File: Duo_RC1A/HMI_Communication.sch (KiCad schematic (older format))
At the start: 24 parts, among them P1 HEADER_180_2.54_10X2, U1 SN75176BDR

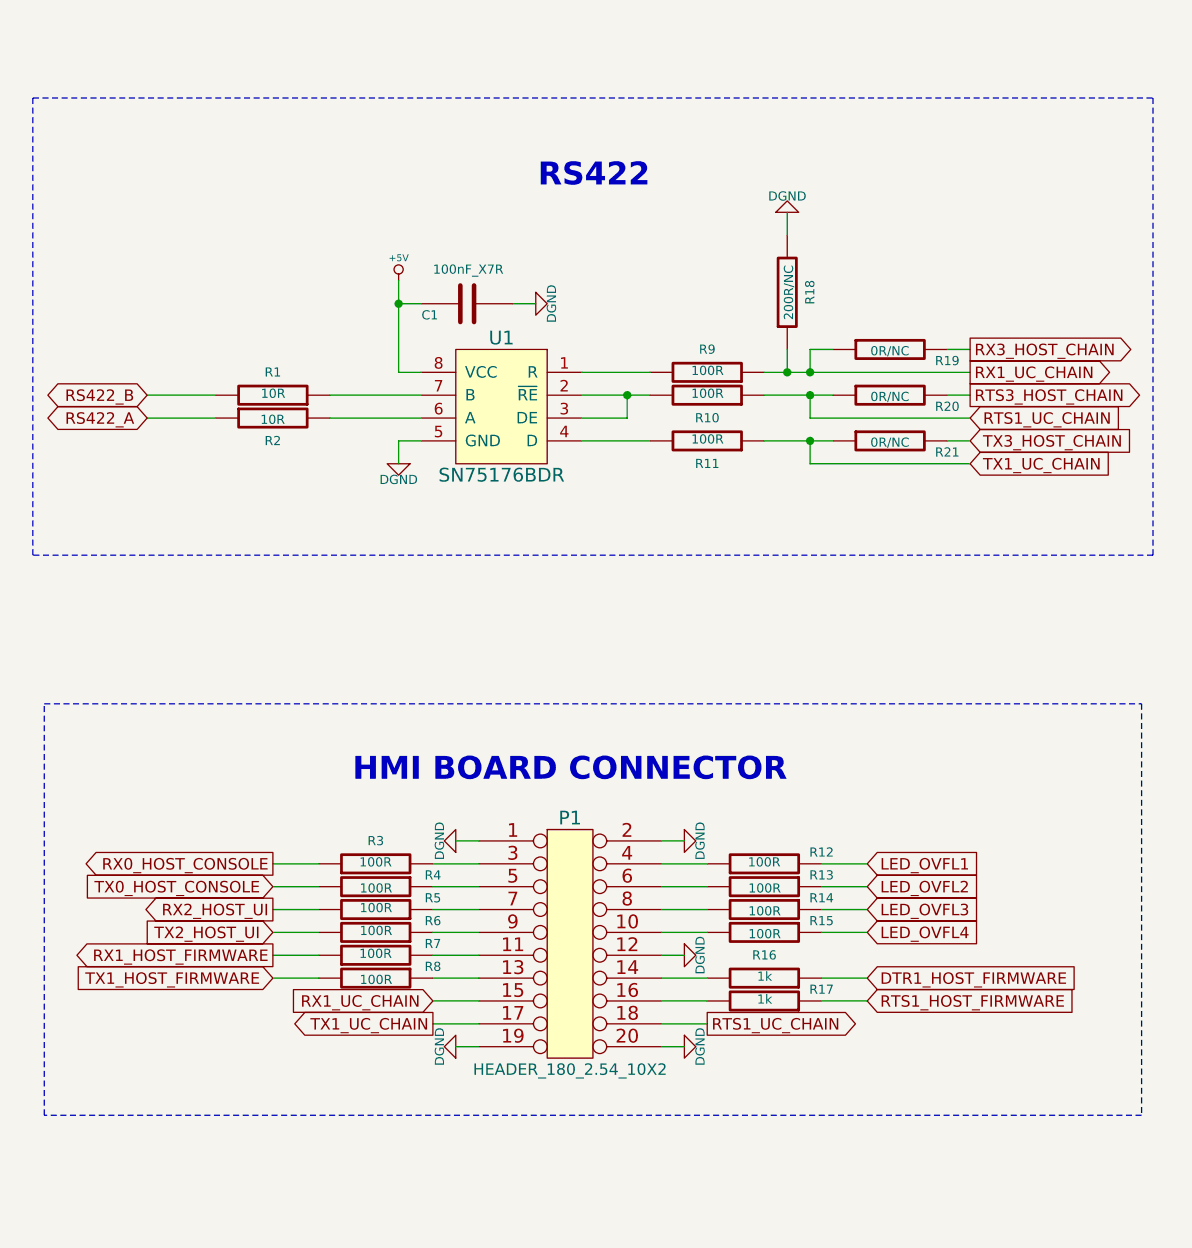
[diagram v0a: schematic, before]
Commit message: Working on the BottomBoard layout. Moved the ITEAD Coreboard to the board left side so there is more space for the linear regulators. Stopped on the USB OTG and USB Host layout.
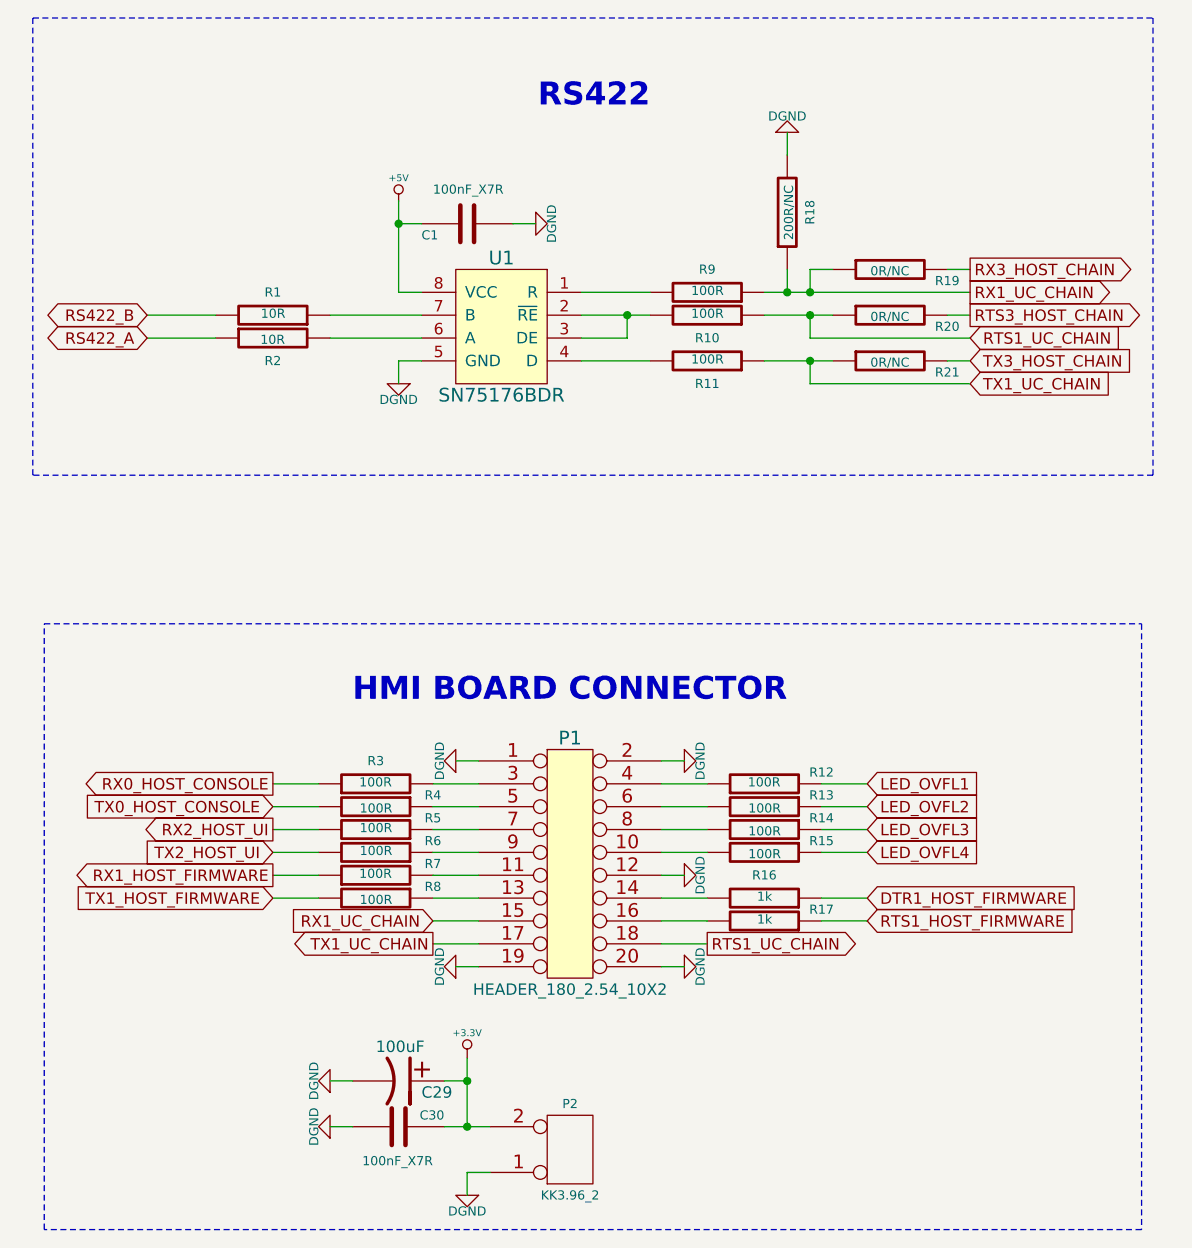
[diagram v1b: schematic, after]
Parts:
- added C29: 100uF, Duo_Audio_HMI_RC1A:Capacitor5x11RM2, symbol CP1
- added C30: 100nF_X7R, Duo_Audio_HMI_RC1A:SM0603, symbol C
- added P2: KK3.96_2, symbol CONN_2
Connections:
- net DGND: now also C29.2, C30.1, P2.1 (P1)
- new net +3.3V: C29.1, C30.2, P2.2 (PM)
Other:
- moved on the sheet: C1, P1, R1, R10, R11, R12, R13, R14, R15, R16, R17, R18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

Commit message: Rear pannel layout finished. First layout of sound modules.
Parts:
- P2: footprint (none) -> Duo_Audio_HMI_RC1A:KK3.96_2PIN
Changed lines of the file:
@@
 F 0 "P2" H 5450 5900 40  0000 C CNN
 F 1 "KK3.96_2" H 5450 6300 40  0000 C CNN
-F 2 "" H 5450 6100 60  0000 C CNN
+F 2 "Duo_Audio_HMI_RC1A:KK3.96_2PIN" H 5450 6100 60  0001 C CNN
 F 3 "" H 5450 6100 60  0000 C CNN
 	1    5450 6100

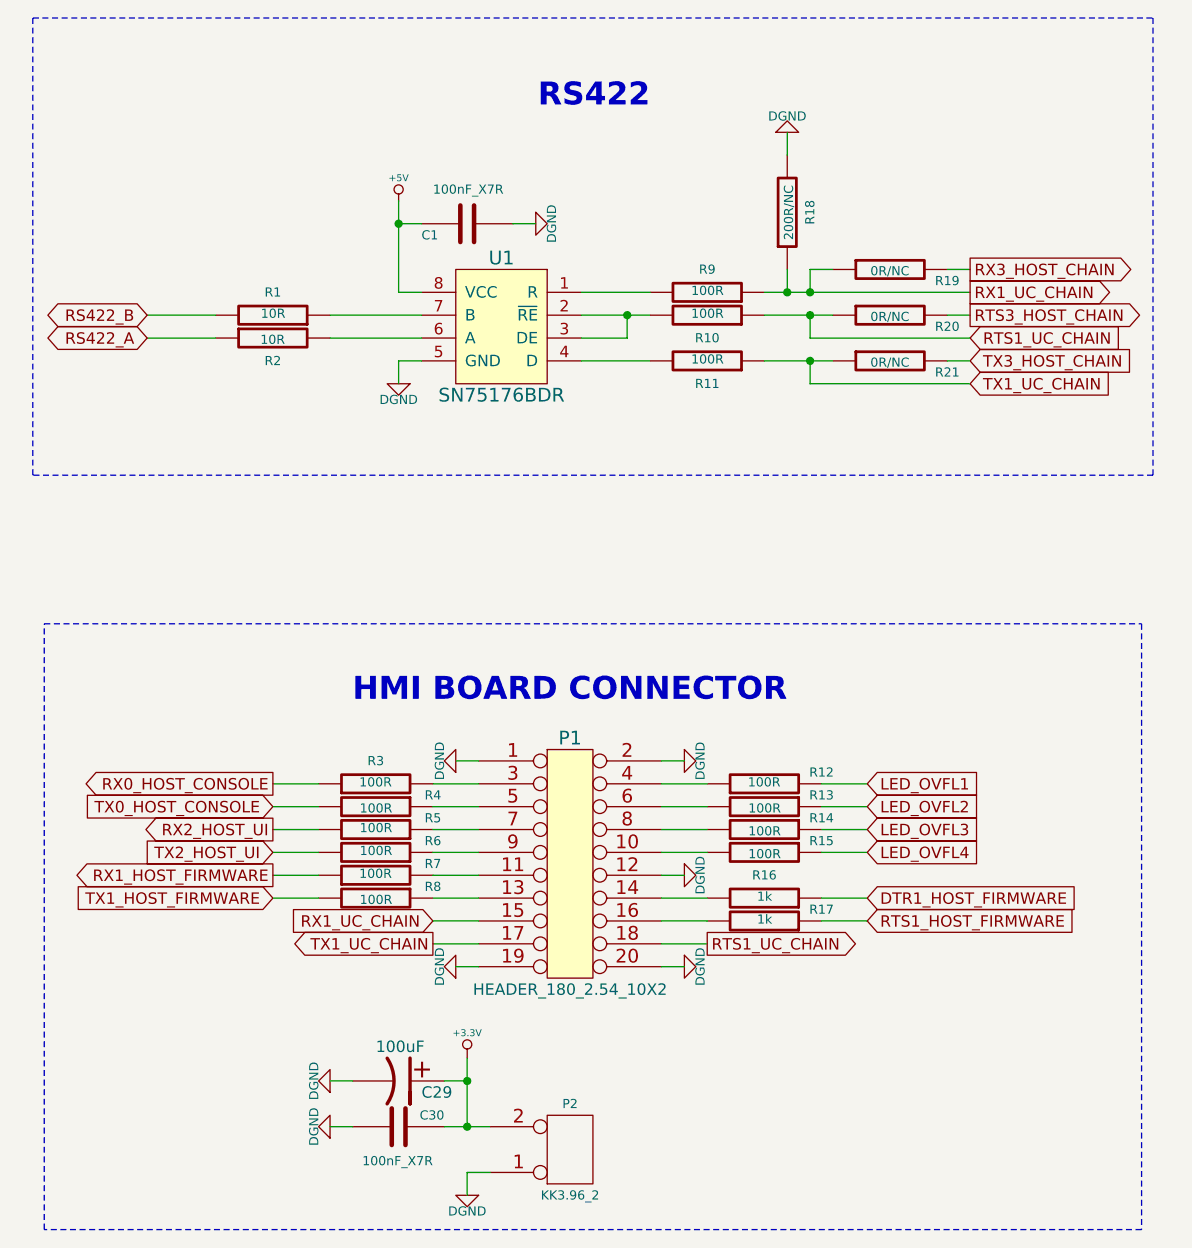
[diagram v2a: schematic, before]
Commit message: Removed CODEC_MITEC signal. Defined the connector between the TopBoard and the BottomBoard. Saved layouts in *.brd old format.
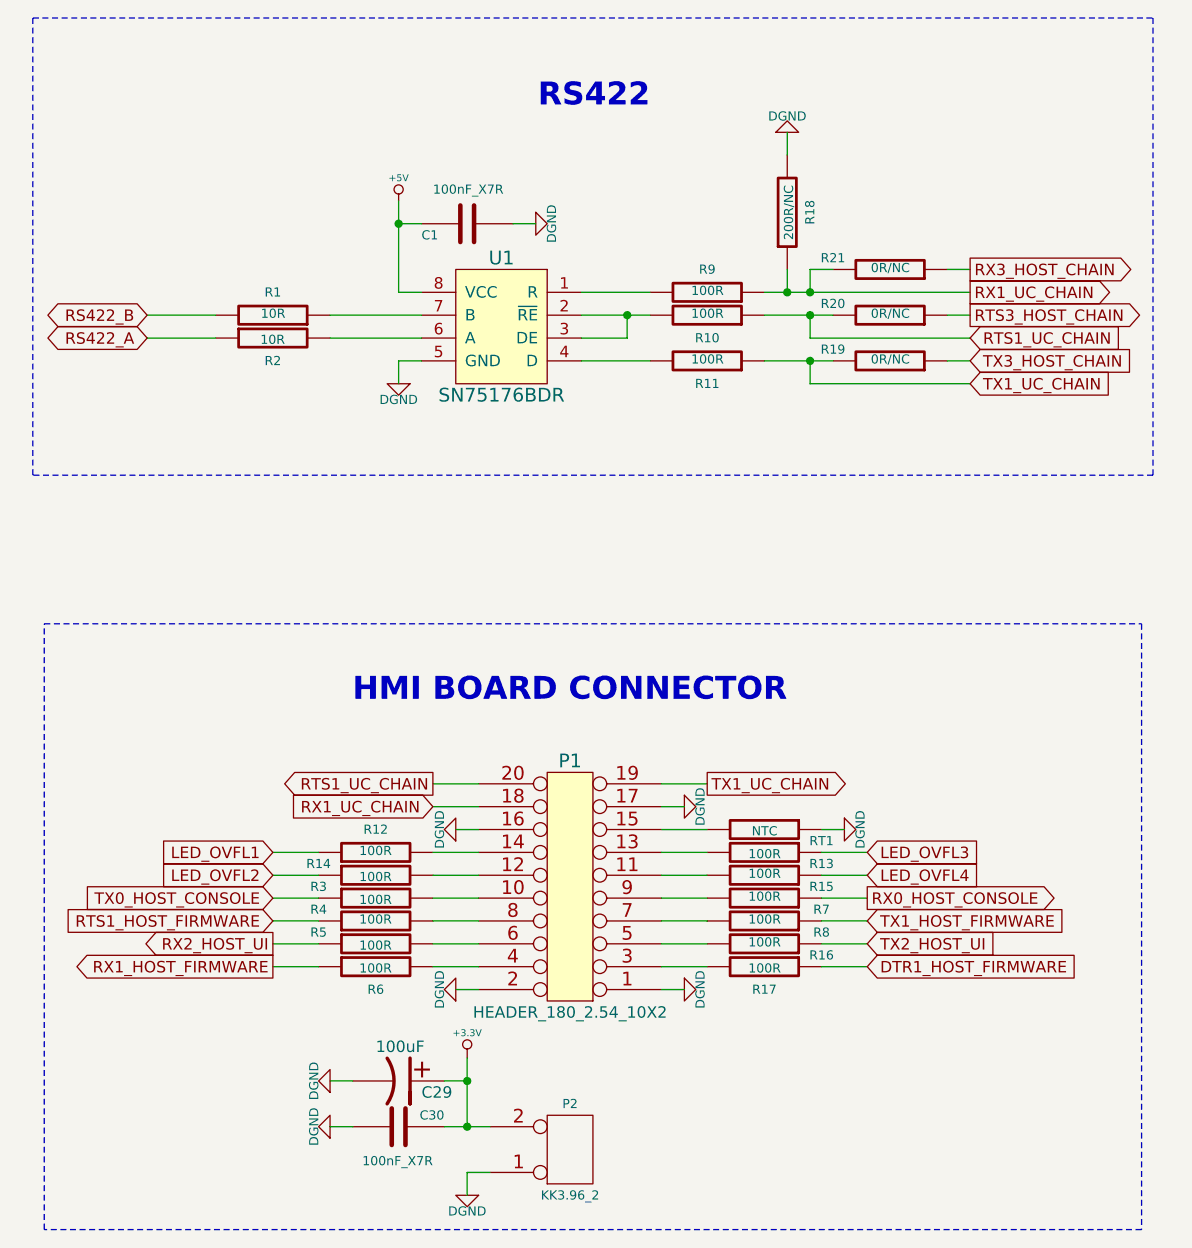
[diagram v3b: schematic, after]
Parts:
- added RT1: NTC, Duo_Audio_HMI_RC1A:SM0805, symbol R
- R16, R17: value 1k -> 100R
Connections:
- net DGND: now also P1.16 (P16), P1.17 (P17), RT1.1; no longer P1.12 (P12), P1.19 (P19), P1.20 (P20)
- net DTR1_HOST_FIRMWARE: now also R17.1; no longer R16.1
- net LED_OVFL1: now also R12.1; no longer R12.2
- net LED_OVFL2: now also R14.1; no longer R13.1
- net LED_OVFL3: now also R13.1; no longer R14.1
- net RTS1_HOST_FIRMWARE: now also R4.1; no longer R17.1
- net RTS1_UC_CHAIN: now also P1.20 (P20), R20.2; no longer P1.18 (P18), R20.1
- net RTS3_HOST_CHAIN: now also R20.1; no longer R20.2
- net RX0_HOST_CONSOLE: now also R7.1; no longer R3.1
- net RX1_HOST_FIRMWARE: now also R6.1; no longer R7.1
- net RX1_UC_CHAIN: now also P1.18 (P18), R21.2; no longer P1.15 (P15), R19.1
- net RX2_HOST_UI: now also R5.1; no longer R5.2
- net RX3_HOST_CHAIN: now also R21.1; no longer R19.2
- net TX0_HOST_CONSOLE: now also R3.1; no longer R4.2
- net TX1_HOST_FIRMWARE: now also R8.1; no longer R8.2
- net TX1_UC_CHAIN: now also P1.19 (P19), R19.2; no longer P1.17 (P17), R21.1
- net TX2_HOST_UI: now also R16.1; no longer R6.2
- net TX3_HOST_CHAIN: now also R19.1; no longer R21.2
- net at P1.11 (P11): now also R15.2; no longer R7.2
- net at P1.13 (P13): now also R13.2; no longer R8.1
- net at R3.2: now also P1.10 (P10); no longer P1.3 (P3)
- net at P1.5 (P5): now also R16.2; no longer R4.1
- net at P1.14 (P14): now also R12.2; no longer R16.2
- net at P1.7 (P7): now also R8.2; no longer R5.1
- net at P1.9 (P9): now also R7.2; no longer R6.1
- net at R17.2: now also P1.3 (P3); no longer P1.16 (P16)
- net at P1.4 (P4): now also R6.2; no longer R12.1
- net at P1.6 (P6): now also R5.2; no longer R13.2
- net at R14.2: now also P1.12 (P12); no longer P1.8 (P8)
- new net: P1.15 (P15), RT1.2
- new net: P1.8 (P8), R4.2
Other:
- moved on the sheet: P1, R12, R13, R14, R15, R19, R21

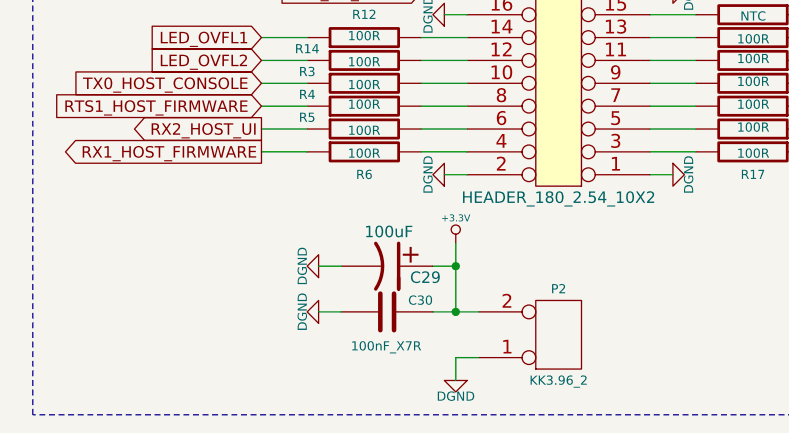
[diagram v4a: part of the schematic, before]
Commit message: Schematic for BOM for ITEAD quote. BottomBoard initial audio placement. Needs to change the ground cuts and the Audio VCC (9V) path.
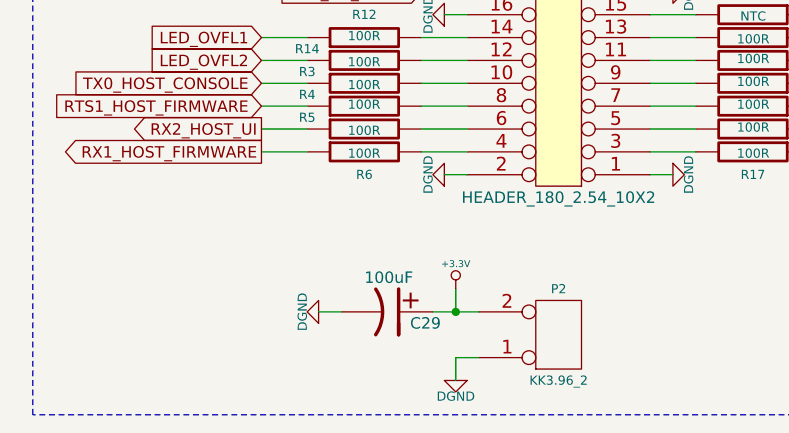
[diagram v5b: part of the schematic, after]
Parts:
- removed C30: 100nF_X7R, Duo_Audio_HMI_RC1A:SM0603, symbol C
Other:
- moved on the sheet: C29
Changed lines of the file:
@@
 $EndComp
 $Comp
-L DGND #PWR9
+L DGND #PWR01
 U 1 1 532173BF
 P 5300 2050
-F 0 "#PWR9" H 5300 2050 40  0001 C CNN
+F 0 "#PWR01" H 5300 2050 40  0001 C CNN
 F 1 "DGND" H 5300 1980 40  0000 C CNN
 F 2 "~" H 5300 2050 60  0000 C CNN
@@
 $EndComp
 $Comp
-L DGND #PWR4
+L DGND #PWR02
 U 1 1 53217476
 P 4700 2750
-F 0 "#PWR4" H 4700 2750 40  0001 C CNN
+F 0 "#PWR02" H 4700 2750 40  0001 C CNN
 F 1 "DGND" H 4700 2680 40  0000 C CNN
 F 2 "~" H 4700 2750 60  0000 C CNN
@@
 	6300 2650 6600 2650
 $Comp
-L +5V #PWR3
+L +5V #PWR03
 U 1 1 5340D40A
 P 4700 1950
-F 0 "#PWR3" H 4700 2040 20  0001 C CNN
+F 0 "#PWR03" H 4700 2040 20  0001 C CNN
 F 1 "+5V" H 4700 2050 30  0000 C CNN
 F 2 "" H 4700 1950 60  0000 C CNN
@@
 $EndComp
 $Comp
-L DGND #PWR12
+L DGND #PWR04
 U 1 1 5373C3D5
 P 6400 1650
-F 0 "#PWR12" H 6400 1650 40  0001 C CNN
+F 0 "#PWR04" H 6400 1650 40  0001 C CNN
 F 1 "DGND" H 6400 1580 40  0000 C CNN
 F 2 "~" H 6400 1650 60  0000 C CNN
@@
 	7100 2650 7200 2650
 $Comp
-L DGND #PWR11
+L DGND #PWR05
 U 1 1 537C830A
 P 5950 5400
-F 0 "#PWR11" H 5950 5400 40  0001 C CNN
+F 0 "#PWR05" H 5950 5400 40  0001 C CNN
 F 1 "DGND" H 5950 5330 40  0000 C CNN
 F 2 "~" H 5950 5400 60  0000 C CNN
@@
 	5950 5400 5850 5400
 $Comp
-L DGND #PWR6
+L DGND #PWR06
 U 1 1 537C8366
 P 4950 5400
-F 0 "#PWR6" H 4950 5400 40  0001 C CNN
+F 0 "#PWR06" H 4950 5400 40  0001 C CNN
 F 1 "DGND" H 4950 5330 40  0000 C CNN
 F 2 "~" H 4950 5400 60  0000 C CNN
@@
 	6050 4500 5850 4500
 $Comp
-L DGND #PWR10
+L DGND #PWR07
 U 1 1 537BED9B
 P 5950 4600
-F 0 "#PWR10" H 5950 4600 40  0001 C CNN
+F 0 "#PWR07" H 5950 4600 40  0001 C CNN
 F 1 "DGND" H 5950 4530 40  0000 C CNN
 F 2 "~" H 5950 4600 60  0000 C CNN
@@
 	5850 4600 5950 4600
 $Comp
-L DGND #PWR5
+L DGND #PWR08
 U 1 1 537BEDA2
 P 4950 4700
-F 0 "#PWR5" H 4950 4700 40  0001 C CNN
+F 0 "#PWR08" H 4950 4700 40  0001 C CNN
 F 1 "DGND" H 4950 4630 40  0000 C CNN
 F 2 "~" H 4950 4700 60  0000 C CNN
@@
 $EndComp
 $Comp
-L +3.3V #PWR7
+L +3.3V #PWR09
 U 1 1 5383BF16
-P 5000 5700
-F 0 "#PWR7" H 5000 5660 30  0001 C CNN
-F 1 "+3.3V" H 5000 5810 30  0000 C CNN
-F 2 "" H 5000 5700 60  0000 C CNN
-F 3 "" H 5000 5700 60  0000 C CNN
-	1    5000 5700
+P 5000 5900
+F 0 "#PWR09" H 5000 5860 30  0001 C CNN
+F 1 "+3.3V" H 5000 6010 30  0000 C CNN
+F 2 "" H 5000 5900 60  0000 C CNN
+F 3 "" H 5000 5900 60  0000 C CNN
+	1    5000 5900
 	1    0    0    -1
 $EndComp
-Wire Wire Line
-	4900 6000 5100 6000
-Wire Wire Line
-	5000 5700 5000 6000
-$Comp
-L DGND #PWR8
+$Comp
+L DGND #PWR010
 U 1 1 5383BFC1
 P 5000 6300
-F 0 "#PWR8" H 5000 6300 40  0001 C CNN
+F 0 "#PWR010" H 5000 6300 40  0001 C CNN
 F 1 "DGND" H 5000 6230 40  0000 C CNN
 F 2 "~" H 5000 6300 60  0000 C CNN
@@
 L CP1 C29
 U 1 1 5383CD1B
-P 4700 5800
-F 0 "C29" V 4750 5900 50  0000 L CNN
-F 1 "100uF" V 4550 5700 50  0000 L CNN
-F 2 "Duo_Audio_HMI_RC1A:Capacitor5x11RM2" H 4700 5800 60  0001 C CNN
-F 3 "" H 4700 5800 60  0000 C CNN
-	1    4700 5800
+P 4700 6000
+F 0 "C29" V 4750 6100 50  0000 L CNN
+F 1 "100uF" V 4550 5900 50  0000 L CNN
+F 2 "Duo_Audio_HMI_RC1A:Capacitor5x11RM2" H 4700 6000 60  0001 C CNN
+F 3 "" H 4700 6000 60  0000 C CNN
+	1    4700 6000
 	0    1    1    0
 $EndComp
-Wire Wire Line
-	4900 5800 5000 5800
-Connection ~ 5000 5800
-$Comp
-L C C30
-U 1 1 5383CDB7
-P 4700 6000
-F 0 "C30" V 4650 5800 40  0000 L CNN
-F 1 "100nF_X7R" V 4850 5850 40  0000 L CNN
-F 2 "Duo_Audio_HMI_RC1A:SM0603" H 4738 5850 30  0001 C CNN
-F 3 "~" H 4700 6000 60  0000 C CNN
-	1    4700 6000
-	0    -1   1    0
-$EndComp
 Connection ~ 5000 6000
 $Comp
-L DGND #PWR1
+L DGND #PWR011
 U 1 1 5383CE13
-P 4400 5800
-F 0 "#PWR1" H 4400 5800 40  0001 C CNN
-F 1 "DGND" H 4400 5730 40  0000 C CNN
-F 2 "~" H 4400 5800 60  0000 C CNN
-F 3 "~" H 4400 5800 60  0000 C CNN
-	1    4400 5800
-	0    1    -1   0
-$EndComp
-$Comp
-L DGND #PWR2
-U 1 1 5383CE1E
 P 4400 6000
-F 0 "#PWR2" H 4400 6000 40  0001 C CNN
+F 0 "#PWR011" H 4400 6000 40  0001 C CNN
 F 1 "DGND" H 4400 5930 40  0000 C CNN
 F 2 "~" H 4400 6000 60  0000 C CNN
@@
 $EndComp
 Wire Wire Line
-	4400 5800 4500 5800
-Wire Wire Line
-	4500 6000 4400 6000
+	4400 6000 4500 6000
 Wire Notes Line
 	7950 3800 7950 6450
@@
 $EndComp
 $Comp
-L DGND #PWR13
+L DGND #PWR012
 U 1 1 53879D52
 P 6650 4700
-F 0 "#PWR13" H 6650 4700 40  0001 C CNN
+F 0 "#PWR012" H 6650 4700 40  0001 C CNN
 F 1 "DGND" H 6650 4630 40  0000 C CNN
 F 2 "~" H 6650 4700 60  0000 C CNN
@@
 Wire Wire Line
 	6550 4700 6650 4700
+Wire Wire Line
+	4900 6000 5100 6000
+Wire Wire Line
+	5000 5900 5000 6000
 $EndSCHEMATC
